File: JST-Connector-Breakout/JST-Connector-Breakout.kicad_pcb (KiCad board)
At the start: 2 copper layers, 90 x 66 mm, 28 parts, among them CN1 JST SHD 2x08, CN10 JST GH 1x06, CN2 JST GH 1x03, CN3 JST GH 1x08, CN5 JST GH 1x02, CN6 JST GH 1x03, CN7 JST XH 1x02, CN8 JST SHD 2x08, CN9 JST GH 1x03, J1 Conn_01x02_Pin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

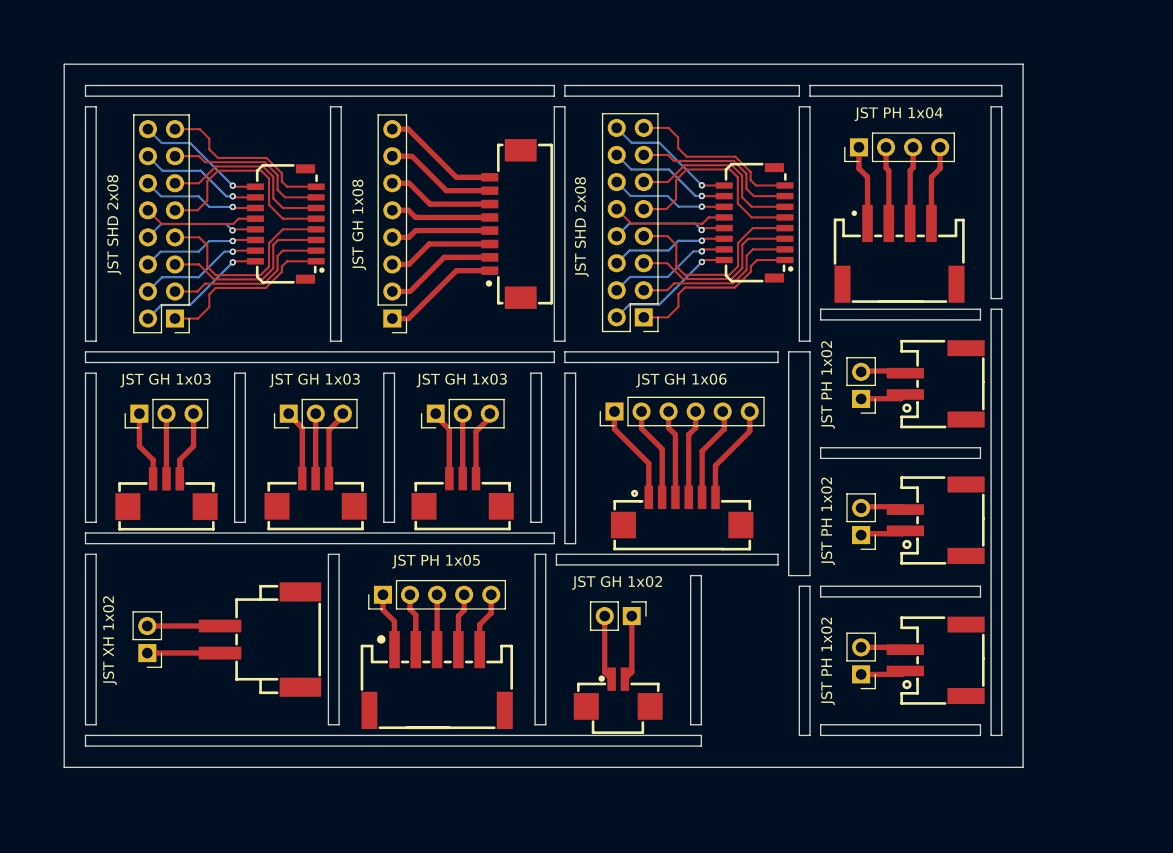
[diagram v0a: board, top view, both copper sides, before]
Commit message: PCB panelizing with mouse bites
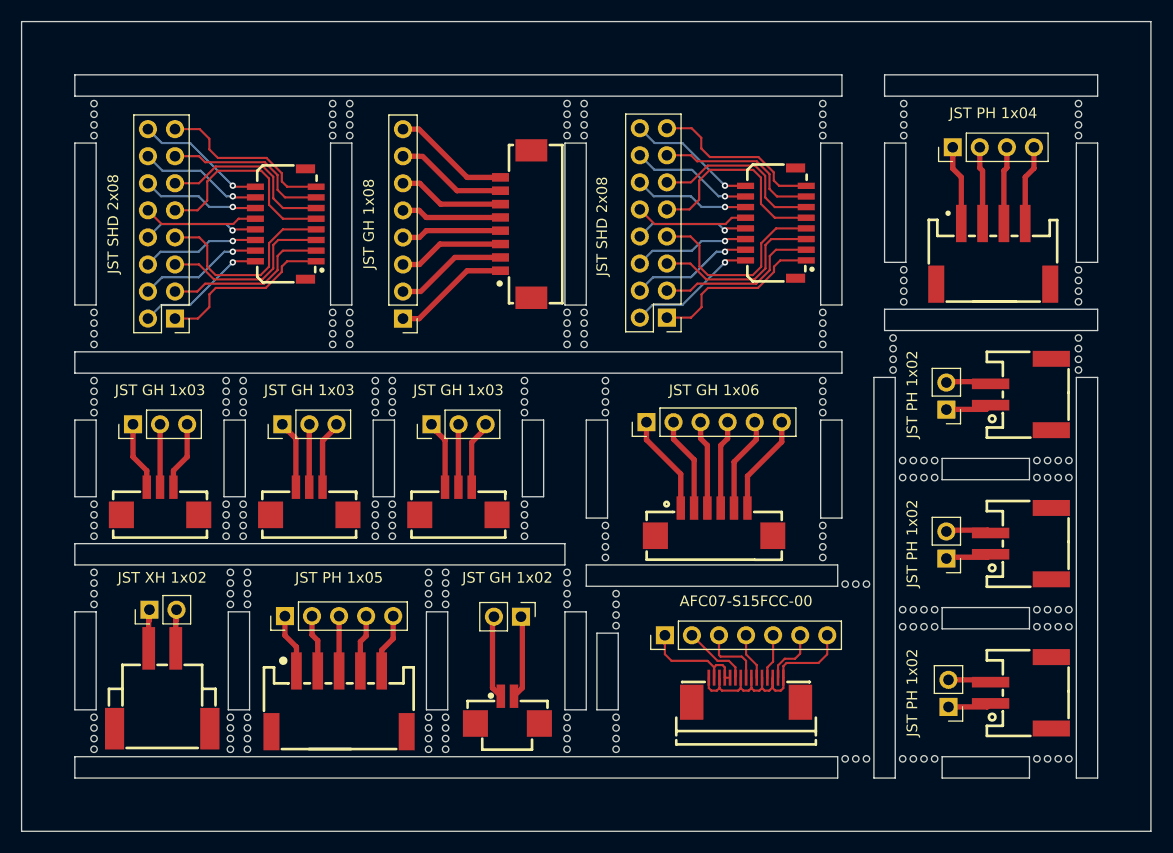
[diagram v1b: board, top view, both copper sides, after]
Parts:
- added FPC1: AFC07-S15FCC-00, easyeda2kicad:FPC-SMD_AFC07-S15FCC-00, F.Cu at (94.2, 85.9)
- added J16: Conn_01x07_Pin, Connector_PinHeader_2.54mm:PinHeader_1x07_P2.54mm_Vertical, F.Cu at (86.6, 80.8)
- moved CN5 10.5 mm to (71.8, 87.8)
- moved J1 10.4 mm to (73.1, 79.1)
- moved CN7 10.3 mm to (39.4, 85.8), turned to 0 degrees
- moved U8 9.41 mm to (56.0, 87.0)
- moved J7 9.41 mm to (50.9, 79.0)
- moved U4 8.80 mm to (117.4, 45.0)
- moved J4 8.80 mm to (113.6, 35.0)
- moved J12 8.75 mm to (113.2, 87.5)
- moved H3 8.56 mm to (120.0, 86.2)
- moved H2 8.30 mm to (120.0, 72.2)
- moved J10 8.30 mm to (113.0, 73.6)
- moved H1 8.06 mm to (120.0, 58.2)
- moved J11 8.06 mm to (113.0, 59.6)
- moved J3 4.08 mm to (38.2, 78.4), turned to 90 degrees
- moved CN10 3.16 mm to (91.2, 70.2)
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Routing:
- net /GND: track 0.00 -> 23.4 mm
- net /VCC: track 0.00 -> 11.5 mm
- net /CS: track 0.00 -> 6.30 mm
- net /DATA: track 0.00 -> 6.21 mm
- net /DC: track 0.00 -> 5.41 mm
- net /CLK: track 0.00 -> 4.40 mm
- net /RESET: track 0.00 -> 4.21 mm
- net Net-(J1-Pin_2): track 6.19 -> 7.84 mm
- net Net-(J1-Pin_1): track 6.19 -> 7.84 mm
- net Net-(J3-Pin_2): track 6.83 -> 5.66 mm
- net Net-(J3-Pin_1): track 6.83 -> 5.66 mm
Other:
- board size 90 x 66 mm -> 106 x 76 mm

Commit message: Refine BOM and fabrication settings for JST breakout
- Exclude non-fitted/connector parts from BOM (in_bom no)
- Add Mfr. Part # for JST connector
- Auto-place schematic net labels
- Enable EXCLUDE DNP in fabrication toolkit
- Regenerate production gerbers and add design backups
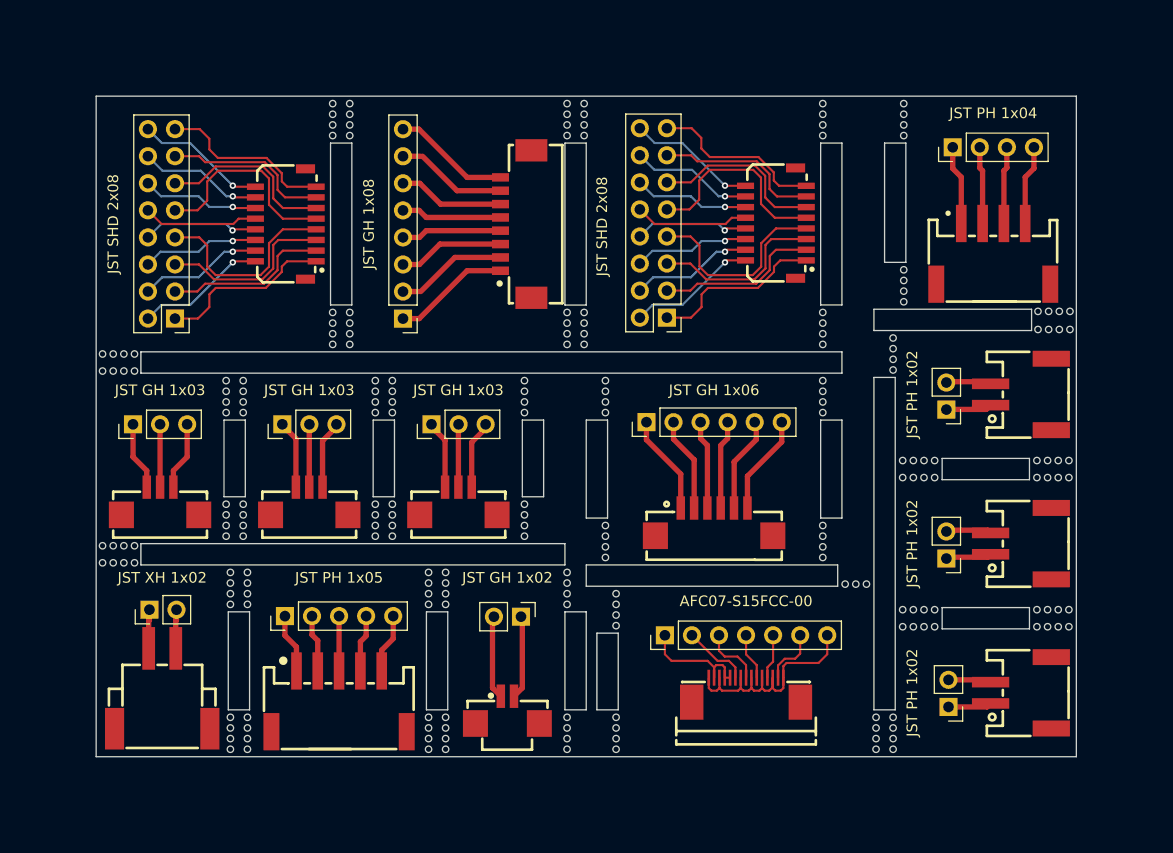
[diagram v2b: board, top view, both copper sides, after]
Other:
- board size 106 x 76 mm -> 92 x 62 mm
